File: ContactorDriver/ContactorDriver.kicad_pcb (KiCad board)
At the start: 2 copper layers, 50 x 40 mm, 18 parts, among them J1 PowerConn, J2 DashboardConn, J3 ContactorConn, Q1 CSD18511KTT

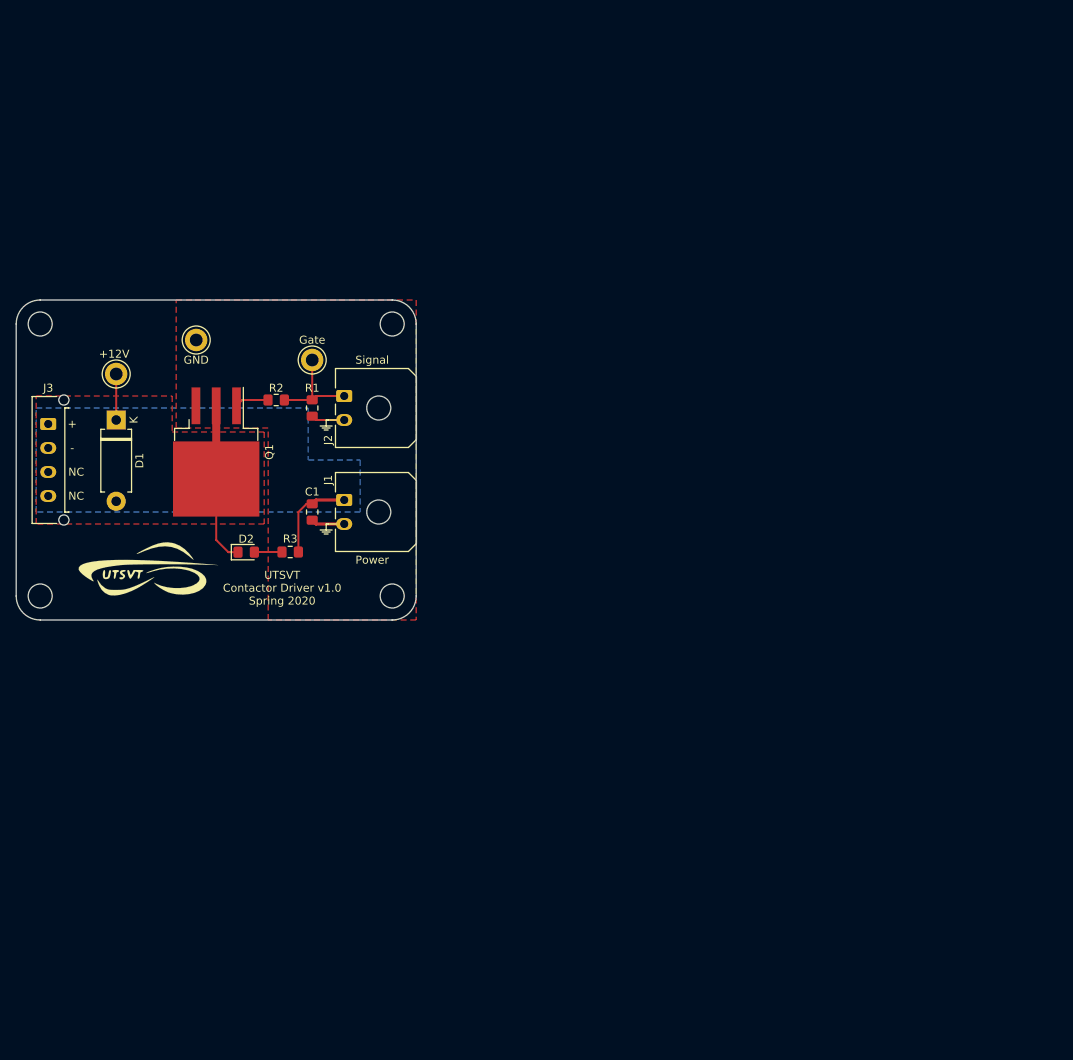
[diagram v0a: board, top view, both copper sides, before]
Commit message: Adds BPS master board with no temperature brd electronics and ContactorDriver for dashboard to control.
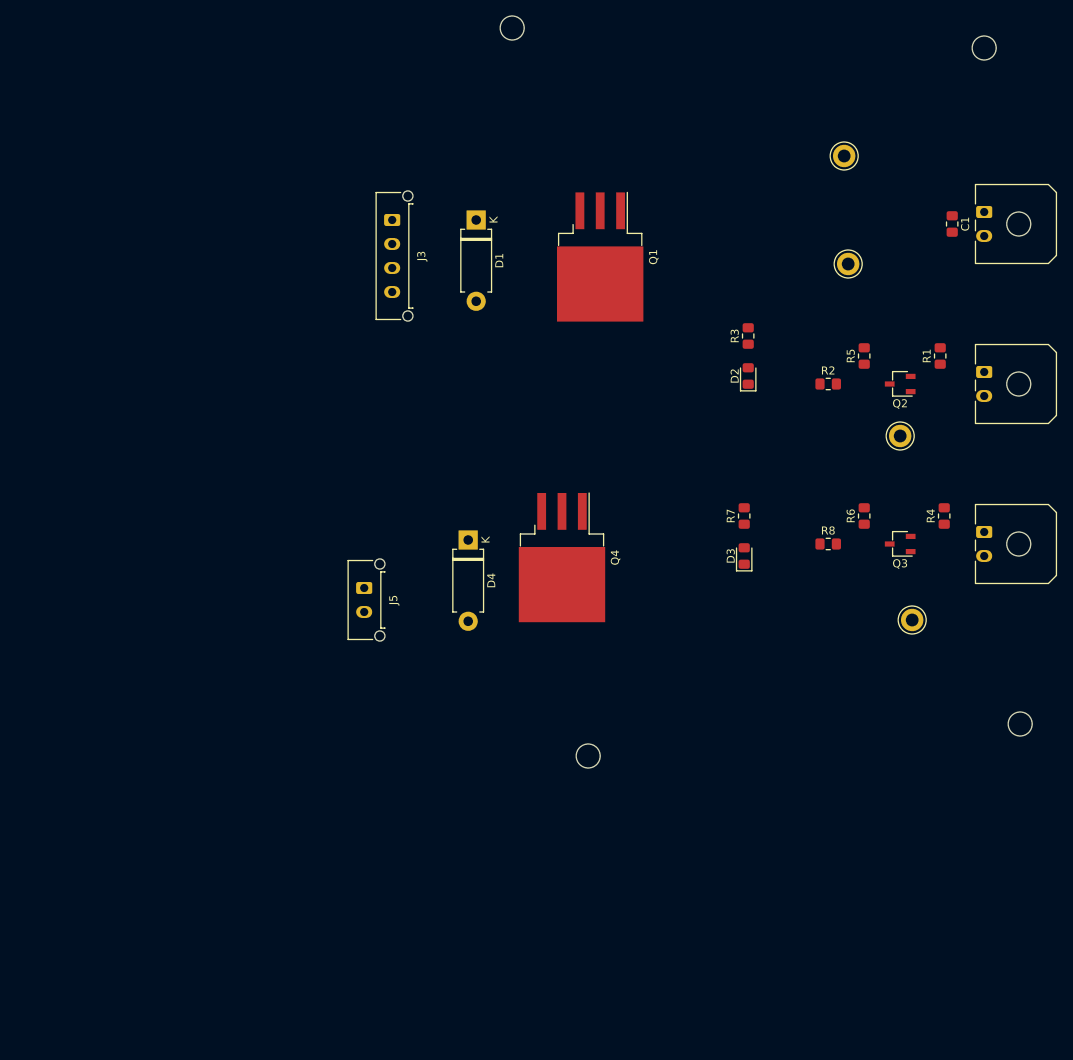
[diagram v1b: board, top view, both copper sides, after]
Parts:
- removed G***: LOGO, UTSVT_Special:UTSVT_Logo_Symbol
- added D3: Green, LED_SMD:LED_0805_2012Metric_Pad1.15x1.40mm_HandSolder, F.Cu at (191.0, 107.0)
- added D4: R5000F, Diode_THT:D_DO-15_P10.16mm_Horizontal, F.Cu at (156.5, 105.0)
- added J4: DashboardConn, Connector_Molex:Molex_Micro-Fit_3.0_43650-0200_1x02_P3.00mm_Horizontal, F.Cu at (221.0, 104.0)
- added J5: PrechargeConn, Connector_Molex:Molex_Micro-Fit_3.0_43650-0215_1x02_P3.00mm_Vertical, F.Cu at (143.5, 111.0)
- added Q2: NTR4003NT1G, Package_TO_SOT_SMD:TSOT-23, F.Cu at (210.5, 85.5)
- added Q3: NTR4003NT1G, Package_TO_SOT_SMD:TSOT-23, F.Cu at (210.5, 105.5)
- added Q4: CSD18511KTT, Package_TO_SOT_SMD:TO-263-3_TabPin2, F.Cu at (168.2, 107.2)
- added R4: 10k, Resistor_SMD:R_0805_2012Metric_Pad1.15x1.40mm_HandSolder, F.Cu at (216.0, 102.0)
- added R5: 10k, Resistor_SMD:R_0805_2012Metric_Pad1.15x1.40mm_HandSolder, F.Cu at (206.0, 82.0)
- added R6: 10k, Resistor_SMD:R_0805_2012Metric_Pad1.15x1.40mm_HandSolder, F.Cu at (206.0, 102.0)
- added R7: 10k, Resistor_SMD:R_0805_2012Metric_Pad1.15x1.40mm_HandSolder, F.Cu at (191.0, 102.0)
- added R8: 0, Resistor_SMD:R_0805_2012Metric_Pad1.15x1.40mm_HandSolder, F.Cu at (201.5, 105.5)
- added TP4: TP_Gate, TestPoint:TestPoint_Keystone_5005-5009_Compact, F.Cu at (212.0, 115.0)
- moved H3 136.4 mm to (221.0, 43.5)
- moved H1 132.3 mm to (225.5, 128.0)
- moved TP2 95.0 mm to (203.5, 57.0)
- moved C1 87.7 mm to (217.0, 65.5)
- moved J1 87.7 mm to (221.0, 64.0)
- moved TP3 82.1 mm to (204.0, 70.5)
- moved J2 80.1 mm to (221.0, 84.0)
- moved R1 78.8 mm to (215.5, 82.0)
- moved TP1 74.1 mm to (210.5, 92.0)
- moved R2 69.0 mm to (201.5, 85.5)
- moved D2 66.5 mm to (191.5, 84.5), turned to 90 degrees
- moved R3 63.3 mm to (191.5, 79.5), turned to 90 degrees
- moved Q1 53.8 mm to (173.0, 69.6)
- moved D1 51.5 mm to (157.5, 65.0)
- moved J3 50.0 mm to (147.0, 65.0)
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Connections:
- R1 pad 1: GND -> Net-(J2-Pad1)
- R1 pad 2: Net-(J2-Pad1) -> +12V
- R2 pad 2: Net-(J2-Pad1) -> Net-(Q2-Pad3)
- TP1 pad 1: Net-(J2-Pad1) -> Net-(Q2-Pad3)
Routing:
- net Net-(D1-Pad2): track 20.1 -> 0.00 mm
- net +12V: track 17.1 -> 0.00 mm
- net Net-(J2-Pad1): track 12.7 -> 0.00 mm
- net GND: track 8.39 -> 0.00 mm
- net Net-(Q1-Pad1): track 4.24 -> 0.00 mm
- net Net-(D2-Pad2): track 3.46 -> 0.00 mm
- removed copper zone on B.Cu, net +12V
- removed copper zone on F.Cu, net GND
- removed copper zone on F.Cu, net Net-(D1-Pad2)
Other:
- board outline removed
- board text removed: "+"
- board text removed: "+12V"
- board text removed: "-"
- board text removed: "34mm"
- board text removed: "44mm"
- board text removed: "GND"
- board text removed: "Gate"
- board text removed: "NC"
- board text removed: "Power"
- board text removed: "Signal"
- board text removed: "UTSVT Contactor Driver v1.0 Spring 2020"

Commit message: Adds resistor mount. Need to add pheonix connector.
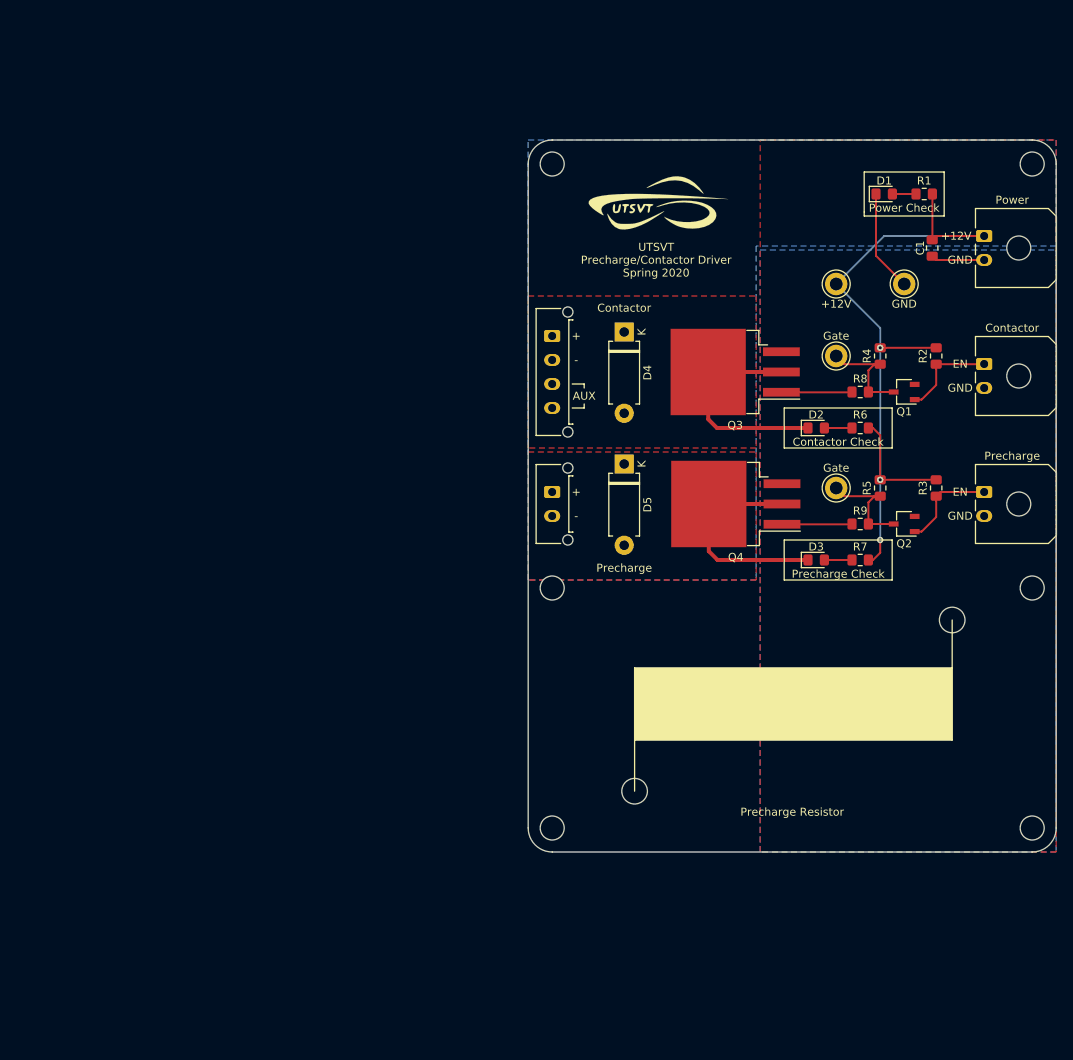
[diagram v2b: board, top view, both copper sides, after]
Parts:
- added D1: Green, LED_SMD:LED_0805_2012Metric_Pad1.15x1.40mm_HandSolder, F.Cu at (208.5, 61.8)
- added G***: LOGO, UTSVT_Special:Hallock_Image, B.Cu at (203.0, 128.5)
- added G***: LOGO, UTSVT_Special:UTSVT_Logo_Symbol, F.Cu at (180.0, 63.0)
- added H1: M4, MountingHole:MountingHole_3.2mm_M3, F.Cu at (177.3, 136.4)
- added H2: M4, MountingHole:MountingHole_3.2mm_M3, F.Cu at (217.0, 115.0)
- added H7: M3, MountingHole:MountingHole_3mm, F.Cu at (227.0, 111.0)
- added H8: M3, MountingHole:MountingHole_3mm, F.Cu at (167.0, 58.0)
- added R1: 10k, Resistor_SMD:R_0805_2012Metric_Pad1.15x1.40mm_HandSolder, F.Cu at (213.5, 61.8)
- H3: renamed from H1; value MountingHole -> M3
- H4: renamed from H2; value MountingHole -> M3
- H5: renamed from H3; value MountingHole -> M3
- H6: renamed from H4; value MountingHole -> M3
- moved H6 70.2 mm to (167.0, 111.0)
- moved J5 26.4 mm to (167.0, 99.0)
- moved J4 24.7 mm to (167.0, 79.5)
- moved D4 23.2 mm to (176.0, 79.0)
- moved Q4 22.7 mm to (189.9, 100.5), turned to 180 degrees
- moved Q3 22.2 mm to (189.9, 84.0), turned to 180 degrees
- moved D5 21.7 mm to (176.0, 95.5)
- moved TP2 19.0 mm to (202.5, 98.5)
- moved R6 18.1 mm to (205.5, 91.0), turned to 0 degrees
- moved TP3 16.0 mm to (202.5, 73.0)
- moved H5 15.7 mm to (227.0, 58.0)
- moved R7 15.5 mm to (205.5, 107.5), turned to 0 degrees
- moved H3 13.1 mm to (227.0, 141.0)
- moved TP1 12.8 mm to (202.5, 82.0)
- moved D2 10.7 mm to (200.0, 91.0), turned to 0 degrees
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- renumbered D1 to D4, D4 to D5, J4 to J3, J3 to J4, Q2 to Q1, Q3 to Q2, Q1 to Q3, R1 to R2, R4 to R3, R5 to R4, R6 to R5, R3 to R6, R2 to R8, R8 to R9, TP4 to TP2, TP2 to TP3, TP3 to TP4
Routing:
- net +12V: track 0.00 -> 92.6 mm, vias 0 -> 3
- net Net-(D2-Pad1): track 0.00 -> 28.0 mm
- net Net-(D3-Pad1): track 0.00 -> 27.9 mm
- net GND: track 0.00 -> 19.4 mm
- net Net-(Q2-Pad3): track 0.00 -> 13.6 mm
- net Net-(Q1-Pad3): track 0.00 -> 13.6 mm
- net Net-(J3-Pad1): track 0.00 -> 12.3 mm
- net Net-(J2-Pad1): track 0.00 -> 12.1 mm
- net Net-(Q3-Pad1): track 0.00 -> 8.84 mm
- net Net-(Q4-Pad1): track 0.00 -> 8.77 mm
- net Net-(D3-Pad2): track 0.00 -> 3.45 mm
- net Net-(D2-Pad2): track 0.00 -> 3.45 mm
- net Net-(D1-Pad2): track 0.00 -> 2.95 mm
- added copper zone on B.Cu, net +12V
- added copper zone on B.Cu, net GND
- added copper zone on F.Cu, net GND
- added copper zone on F.Cu, net Net-(D2-Pad1)
- added copper zone on F.Cu, net Net-(D3-Pad1)
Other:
- board outline added: 66 x 89 mm
- board text added: "+"
- board text added: "+12V"
- board text added: "-"
- board text added: "30mm"
- board text added: "53mm"
- board text added: "60mm"
- board text added: "AUX"
- board text added: "Contactor"
- board text added: "Contactor Check"
- board text added: "Dr. Gary Hallock"
- board text added: "EN"
- board text added: "GND"
- board text added: "Gate"
- board text added: "Power"
- board text added: "Power Check"
- board text added: "Precharge"
- board text added: "Precharge Check"
- board text added: "Precharge Resistor"
- board text added: "UTSVT Precharge/Contactor Driver Spring 2020"

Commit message: Adds final BPS leader board and completed Contactor/precharge board.
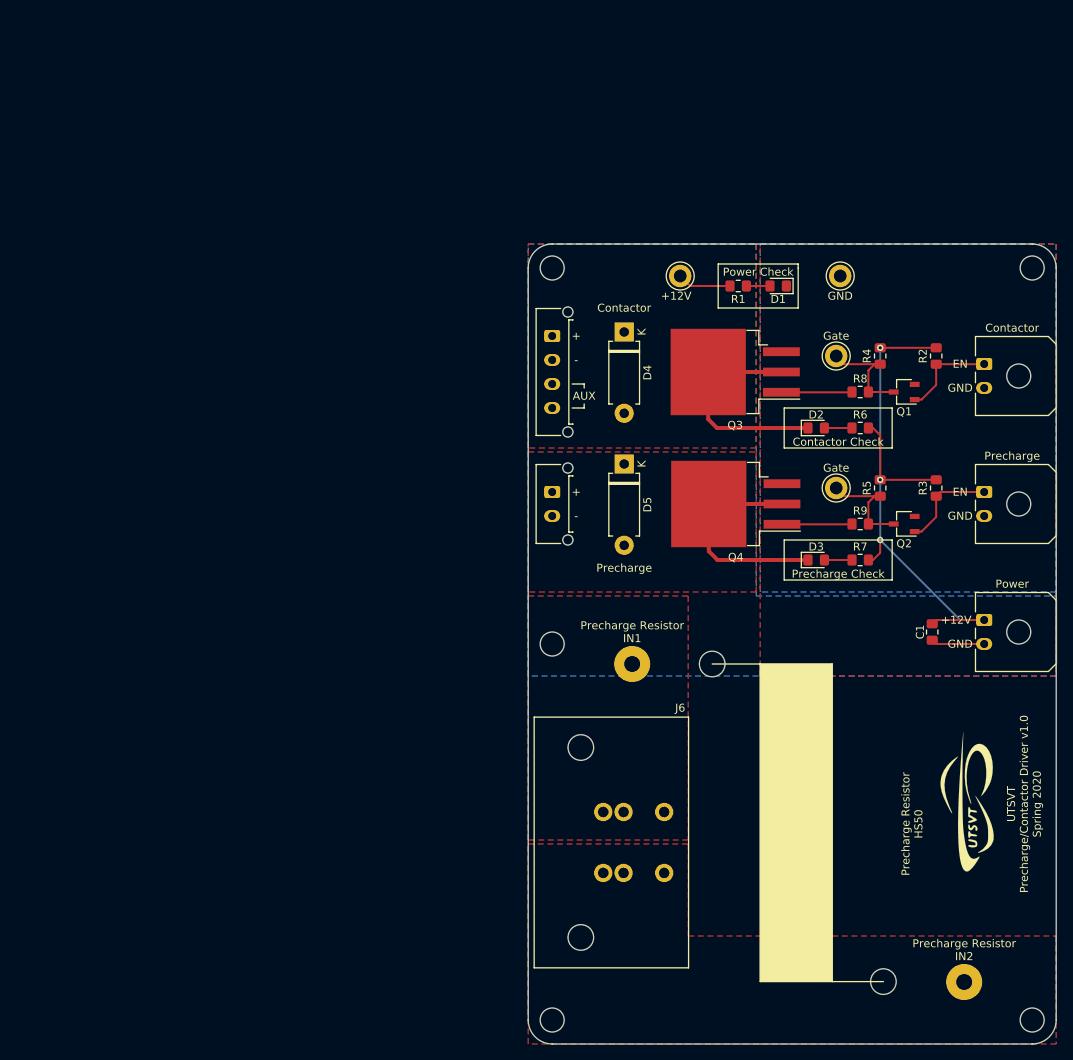
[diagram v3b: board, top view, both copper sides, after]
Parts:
- removed H8: M3, MountingHole:MountingHole_3mm
- added J6: PrechargeResistorConn, UTSVT_Connectors:PhoenixContact_PowerCombicon5_GF_2x7.62mm, F.Cu at (181.0, 139.0)
- added J7: PrechargeResistor, Connector_Wire:SolderWirePad_1x01_Drill2mm, F.Cu at (177.0, 120.5)
- added J8: PrechargeResistor, Connector_Wire:SolderWirePad_1x01_Drill2mm, F.Cu at (218.5, 160.2)
- moved G*** 84.5 mm to (219.0, 138.0), turned to 90 degrees
- moved H7 60.4 mm to (167.0, 118.0)
- moved C1 48.0 mm to (214.5, 116.5)
- moved J1 48.0 mm to (221.0, 115.0)
- moved H6 40.0 mm to (167.0, 71.0)
- moved H1 39.2 mm to (208.4, 160.2), turned to 180 degrees
- moved H2 30.5 mm to (187.0, 120.5), turned to 180 degrees
- moved R1 25.9 mm to (190.2, 73.2), turned to 180 degrees
- moved H3 24.0 mm to (227.0, 165.0)
- moved H4 24.0 mm to (167.0, 165.0)
- moved TP3 19.5 mm to (183.0, 72.0)
- moved D1 17.5 mm to (195.2, 73.2), turned to 180 degrees
- moved H5 13.0 mm to (227.0, 71.0)
- moved TP4 8.06 mm to (203.0, 72.0)
- moved G*** 6.80 mm to (199.0, 134.0), turned to 180 degrees
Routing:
- net +12V: track 92.6 -> 79.5 mm
- net GND: track 19.4 -> 6.70 mm
- added copper zone on F.Cu, net Net-(J6-Pad1)
- added copper zone on F.Cu, net Net-(J6-Pad2)
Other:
- board size 66 x 89 mm -> 66 x 100 mm
- board text added: "Precharge Resistor HS50"
- board text added: "Precharge Resistor IN1"
- board text added: "Precharge Resistor IN2"
- board text added: "UTSVT Precharge/Contactor Driver v1.0 Spring 2020"
- board text removed: "30mm"
- board text removed: "53mm"
- board text removed: "Precharge Resistor"
- board text removed: "UTSVT Precharge/Contactor Driver Spring 2020"
